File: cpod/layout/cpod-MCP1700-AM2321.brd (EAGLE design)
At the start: 14 parts, among them IC1 PCF8563DIP, Y1 32.768kHz

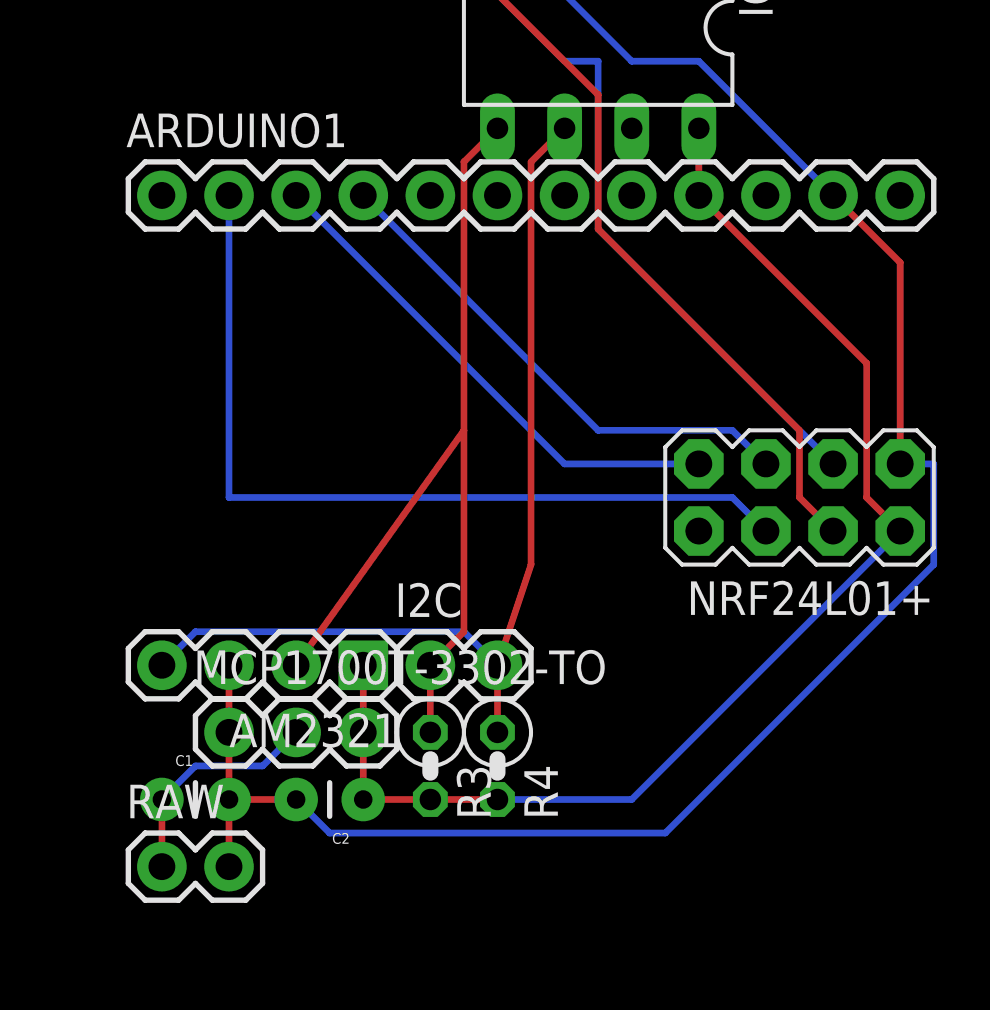
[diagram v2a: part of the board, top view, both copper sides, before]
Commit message: 增加了去耦电容
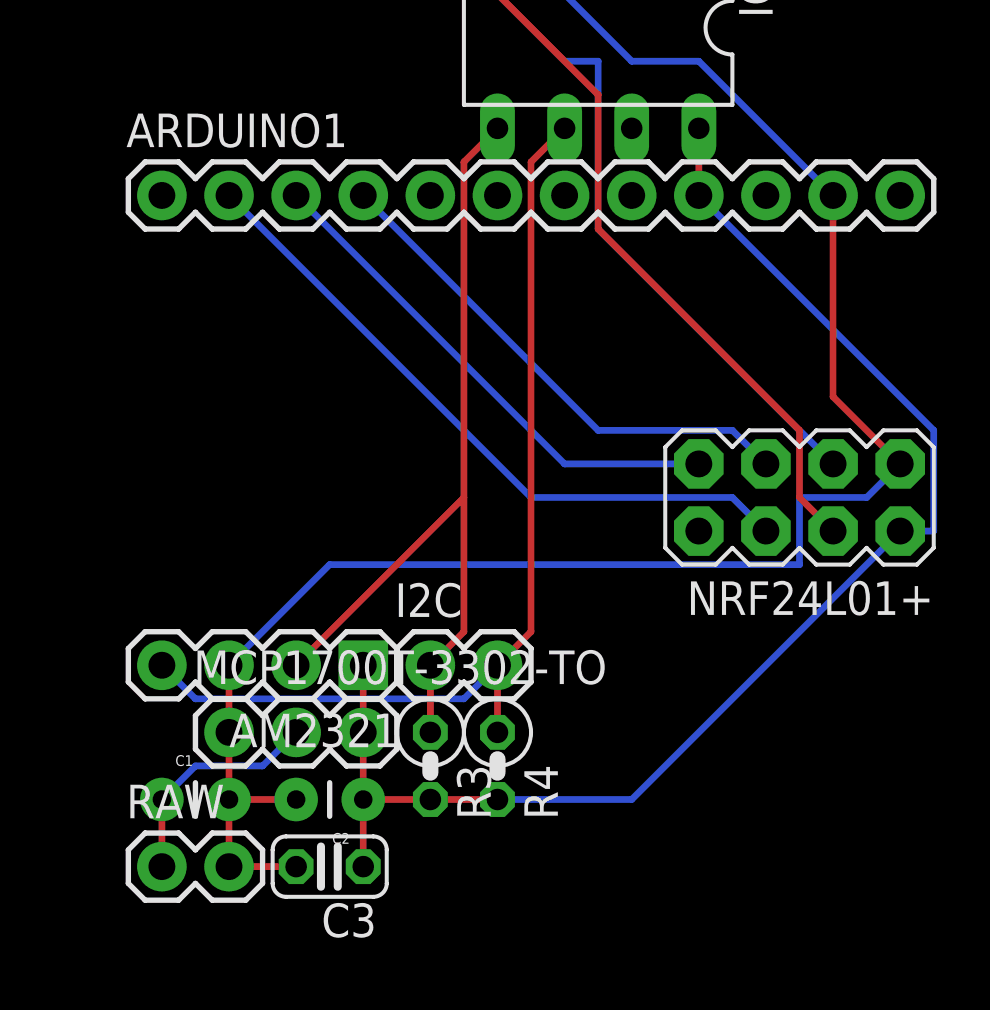
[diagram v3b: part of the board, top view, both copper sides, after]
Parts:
- added C3: 100nF, rcl:C025-024X044
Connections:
- net D3 renamed INT1
- net GND: now also C3.2
- net VCC: now also C3.1
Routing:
- net MOSI: track 32.3 -> 25.6 mm
- net VCC: track 48.0 -> 52.3 mm
- net SDA: track 34.8 -> 32.9 mm
- net GND: track 72.2 -> 70.9 mm
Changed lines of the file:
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@@
 <element name="IC1" library="CEDT" package="DIL08" value="PCF8563DIP" x="48.26" y="-10.16" rot="R180"/>
 <element name="Y1" library="SparkFun-FreqCtrl" package="TC26H" value="32.768kHz" x="50.8" y="-3.81"/>
+<element name="C3" library="rcl" package="C025-024X044" value="100nF" x="38.1" y="-41.91" rot="R180"/>
 </elements>
 <signals>
@@
 <wire x1="44.45" y1="-34.29" x2="44.45" y2="-36.83" width="0.254" layer="1"/>
 <wire x1="45.72" y1="-15.24" x2="46.99" y2="-13.97" width="0.254" layer="1"/>
-<wire x1="45.72" y1="-30.48" x2="45.72" y2="-15.24" width="0.254" layer="1"/>
-<wire x1="44.45" y1="-34.29" x2="45.72" y2="-30.48" width="0.254" layer="1"/>
-<wire x1="33.02" y1="-33.02" x2="31.75" y2="-34.29" width="0.254" layer="16"/>
-<wire x1="43.18" y1="-33.02" x2="33.02" y2="-33.02" width="0.254" layer="16"/>
-<wire x1="44.45" y1="-34.29" x2="43.18" y2="-33.02" width="0.254" layer="16"/>
+<wire x1="45.72" y1="-33.02" x2="45.72" y2="-15.24" width="0.254" layer="1"/>
+<wire x1="44.45" y1="-34.29" x2="45.72" y2="-33.02" width="0.254" layer="1"/>
+<wire x1="33.02" y1="-35.56" x2="31.75" y2="-34.29" width="0.254" layer="16"/>
+<wire x1="43.18" y1="-35.56" x2="33.02" y2="-35.56" width="0.254" layer="16"/>
+<wire x1="44.45" y1="-34.29" x2="43.18" y2="-35.56" width="0.254" layer="16"/>
 </signal>
 <signal name="GND">
@@
 <wire x1="52.07" y1="-11.43" x2="49.53" y2="-11.43" width="0.254" layer="16"/>
 <wire x1="57.15" y1="-16.51" x2="52.07" y2="-11.43" width="0.254" layer="16"/>
-<wire x1="59.69" y1="-19.05" x2="59.69" y2="-26.67" width="0.254" layer="1"/>
-<wire x1="57.15" y1="-16.51" x2="59.69" y2="-19.05" width="0.254" layer="1"/>
-<wire x1="38.1" y1="-40.64" x2="36.83" y2="-39.37" width="0.254" layer="16"/>
-<wire x1="50.8" y1="-40.64" x2="38.1" y2="-40.64" width="0.254" layer="16"/>
-<wire x1="60.96" y1="-30.48" x2="50.8" y2="-40.64" width="0.254" layer="16"/>
-<wire x1="60.96" y1="-26.67" x2="60.96" y2="-30.48" width="0.254" layer="16"/>
-<wire x1="59.69" y1="-26.67" x2="60.96" y2="-26.67" width="0.254" layer="16"/>
+<wire x1="57.15" y1="-24.13" x2="59.69" y2="-26.67" width="0.254" layer="1"/>
+<wire x1="57.15" y1="-16.51" x2="57.15" y2="-24.13" width="0.254" layer="1"/>
+<wire x1="38.1" y1="-30.48" x2="34.29" y2="-34.29" width="0.254" layer="16"/>
+<wire x1="55.88" y1="-30.48" x2="38.1" y2="-30.48" width="0.254" layer="16"/>
+<wire x1="55.88" y1="-27.94" x2="55.88" y2="-30.48" width="0.254" layer="16"/>
+<wire x1="58.42" y1="-27.94" x2="55.88" y2="-27.94" width="0.254" layer="16"/>
+<wire x1="59.69" y1="-26.67" x2="58.42" y2="-27.94" width="0.254" layer="16"/>
+<contactref element="C3" pad="2"/>
+<wire x1="34.29" y1="-41.91" x2="36.83" y2="-41.91" width="0.254" layer="1"/>
 </signal>
 <signal name="SDA">
@@
 <wire x1="41.91" y1="-34.29" x2="41.91" y2="-36.83" width="0.254" layer="1"/>
 <wire x1="43.18" y1="-15.24" x2="44.45" y2="-13.97" width="0.254" layer="1"/>
-<wire x1="43.18" y1="-33.02" x2="43.18" y2="-25.4" width="0.254" layer="1"/>
-<wire x1="43.18" y1="-25.4" x2="43.18" y2="-15.24" width="0.254" layer="1"/>
+<wire x1="43.18" y1="-33.02" x2="43.18" y2="-27.94" width="0.254" layer="1"/>
+<wire x1="43.18" y1="-27.94" x2="43.18" y2="-15.24" width="0.254" layer="1"/>
 <wire x1="41.91" y1="-34.29" x2="43.18" y2="-33.02" width="0.254" layer="1"/>
-<wire x1="43.18" y1="-25.4" x2="36.83" y2="-34.29" width="0.254" layer="1"/>
+<wire x1="43.18" y1="-27.94" x2="36.83" y2="-34.29" width="0.254" layer="1"/>
 </signal>
 <signal name="VCC">
@@
 <wire x1="49.53" y1="-39.37" x2="59.69" y2="-29.21" width="0.254" layer="16"/>
 <wire x1="44.45" y1="-39.37" x2="49.53" y2="-39.37" width="0.254" layer="16"/>
-<wire x1="58.42" y1="-22.86" x2="52.07" y2="-16.51" width="0.254" layer="1"/>
-<wire x1="58.42" y1="-27.94" x2="58.42" y2="-22.86" width="0.254" layer="1"/>
-<wire x1="59.69" y1="-29.21" x2="58.42" y2="-27.94" width="0.254" layer="1"/>
+<wire x1="60.96" y1="-25.4" x2="52.07" y2="-16.51" width="0.254" layer="16"/>
+<wire x1="60.96" y1="-29.21" x2="60.96" y2="-25.4" width="0.254" layer="16"/>
+<wire x1="59.69" y1="-29.21" x2="60.96" y2="-29.21" width="0.254" layer="16"/>
 <wire x1="39.37" y1="-39.37" x2="39.37" y2="-36.83" width="0.254" layer="1"/>
+<contactref element="C3" pad="1"/>
+<wire x1="39.37" y1="-39.37" x2="39.37" y2="-41.91" width="0.254" layer="1"/>
 </signal>
 <signal name="RAW">
@@
 <contactref element="ARDUINO1" pad="2"/>
 <contactref element="NRF24L01+" pad="6"/>
-<wire x1="34.29" y1="-27.94" x2="34.29" y2="-16.51" width="0.254" layer="16"/>
-<wire x1="53.34" y1="-27.94" x2="34.29" y2="-27.94" width="0.254" layer="16"/>
+<wire x1="45.72" y1="-27.94" x2="34.29" y2="-16.51" width="0.254" layer="16"/>
+<wire x1="53.34" y1="-27.94" x2="45.72" y2="-27.94" width="0.254" layer="16"/>
 <wire x1="54.61" y1="-29.21" x2="53.34" y2="-27.94" width="0.254" layer="16"/>
 </signal>
@@
 <contactref element="ARDUINO2" pad="11"/>
 </signal>
-<signal name="D3">
+<signal name="INT1">
 <contactref element="ARDUINO2" pad="7"/>
 </signal>

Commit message: I2C的上拉电阻改到5.1k
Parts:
- R3, R4: value 4.7k -> 5.1k
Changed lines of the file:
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@@
 <element name="RAW" library="SparkFun-Connectors" package="1X02" value="" x="31.75" y="-41.91"/>
 <element name="NRF24L01+" library="SparkFun-Connectors" package="2X4" value="M04X2" x="55.88" y="-27.94" rot="R180"/>
-<element name="R3" library="rcl" package="0207/2V" value="4.7k" x="41.91" y="-38.1" rot="R270"/>
-<element name="R4" library="rcl" package="0207/2V" value="4.7k" x="44.45" y="-38.1" rot="R270"/>
+<element name="R3" library="rcl" package="0207/2V" value="5.1k" x="41.91" y="-38.1" rot="R270"/>
+<element name="R4" library="rcl" package="0207/2V" value="5.1k" x="44.45" y="-38.1" rot="R270"/>
 <element name="I2C" library="SparkFun-Connectors" package="1X02" value="" x="41.91" y="-34.29"/>
 <element name="U$2" library="SparkFun-Aesthetics" package="OSHW-LOGO-L" value="" x="5.08" y="-38.1"/>

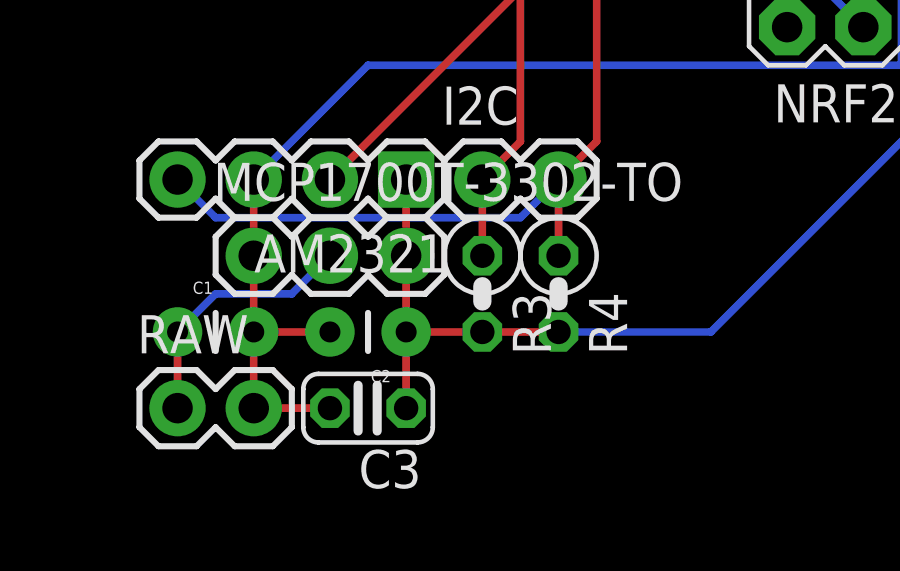
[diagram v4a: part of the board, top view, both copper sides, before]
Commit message: 把去耦放到电源框里，增加表意性。
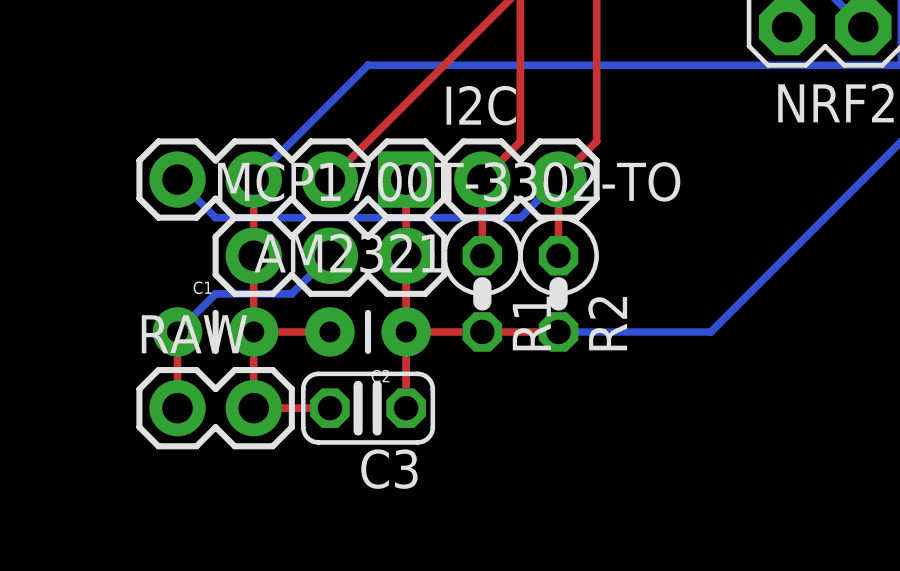
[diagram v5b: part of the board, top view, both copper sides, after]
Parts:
- renumbered R3 to R1, R4 to R2
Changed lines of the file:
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@@
 <element name="RAW" library="SparkFun-Connectors" package="1X02" value="" x="31.75" y="-41.91"/>
 <element name="NRF24L01+" library="SparkFun-Connectors" package="2X4" value="M04X2" x="55.88" y="-27.94" rot="R180"/>
-<element name="R3" library="rcl" package="0207/2V" value="5.1k" x="41.91" y="-38.1" rot="R270"/>
-<element name="R4" library="rcl" package="0207/2V" value="5.1k" x="44.45" y="-38.1" rot="R270"/>
+<element name="R1" library="rcl" package="0207/2V" value="5.1k" x="41.91" y="-38.1" rot="R270"/>
+<element name="R2" library="rcl" package="0207/2V" value="5.1k" x="44.45" y="-38.1" rot="R270"/>
 <element name="I2C" library="SparkFun-Connectors" package="1X02" value="" x="41.91" y="-34.29"/>
 <element name="U$2" library="SparkFun-Aesthetics" package="OSHW-LOGO-L" value="" x="5.08" y="-38.1"/>
@@
 <contactref element="AM2321" pad="4"/>
 <contactref element="I2C" pad="2"/>
-<contactref element="R4" pad="1"/>
+<contactref element="R2" pad="1"/>
 <contactref element="IC1" pad="6"/>
 <wire x1="44.45" y1="-34.29" x2="44.45" y2="-36.83" width="0.254" layer="1"/>
@@
 <contactref element="MCP1700T-3302-TO" pad="1"/>
 <contactref element="C1" pad="2"/>
-<contactref element="C2" pad="2"/>
 <contactref element="AM2321" pad="3"/>
 <contactref element="RAW" pad="2"/>
@@
 <contactref element="ARDUINO1" pad="11"/>
 <wire x1="34.29" y1="-36.83" x2="34.29" y2="-39.37" width="0.254" layer="1"/>
-<wire x1="34.29" y1="-39.37" x2="36.83" y2="-39.37" width="0.254" layer="1"/>
 <wire x1="34.29" y1="-39.37" x2="34.29" y2="-41.91" width="0.254" layer="1"/>
 <wire x1="34.29" y1="-36.83" x2="34.29" y2="-34.29" width="0.254" layer="1"/>
@@
 <wire x1="58.42" y1="-27.94" x2="55.88" y2="-27.94" width="0.254" layer="16"/>
 <wire x1="59.69" y1="-26.67" x2="58.42" y2="-27.94" width="0.254" layer="16"/>
+<contactref element="C2" pad="2"/>
 <contactref element="C3" pad="2"/>
 <wire x1="34.29" y1="-41.91" x2="36.83" y2="-41.91" width="0.254" layer="1"/>
+<wire x1="36.83" y1="-39.37" x2="34.29" y2="-39.37" width="0.254" layer="1"/>
 </signal>
 <signal name="SDA">
 <contactref element="AM2321" pad="2"/>
 <contactref element="I2C" pad="1"/>
-<contactref element="R3" pad="1"/>
+<contactref element="R1" pad="1"/>
 <contactref element="IC1" pad="5"/>
 <wire x1="41.91" y1="-34.29" x2="41.91" y2="-36.83" width="0.254" layer="1"/>
@@
 <contactref element="AM2321" pad="1"/>
 <contactref element="ARDUINO1" pad="9"/>
-<contactref element="C2" pad="1"/>
-<contactref element="R4" pad="2"/>
-<contactref element="R3" pad="2"/>
+<contactref element="R2" pad="2"/>
+<contactref element="R1" pad="2"/>
 <contactref element="NRF24L01+" pad="2"/>
 <contactref element="MCP1700T-3302-TO" pad="3"/>
@@
 <wire x1="39.37" y1="-34.29" x2="39.37" y2="-36.83" width="0.254" layer="1"/>
 <wire x1="52.07" y1="-16.51" x2="52.07" y2="-13.97" width="0.254" layer="1"/>
-<wire x1="39.37" y1="-39.37" x2="41.91" y2="-39.37" width="0.254" layer="1"/>
 <wire x1="41.91" y1="-39.37" x2="44.45" y2="-39.37" width="0.254" layer="1"/>
 <wire x1="49.53" y1="-39.37" x2="59.69" y2="-29.21" width="0.254" layer="16"/>
@@
 <wire x1="60.96" y1="-29.21" x2="60.96" y2="-25.4" width="0.254" layer="16"/>
 <wire x1="59.69" y1="-29.21" x2="60.96" y2="-29.21" width="0.254" layer="16"/>
-<wire x1="39.37" y1="-39.37" x2="39.37" y2="-36.83" width="0.254" layer="1"/>
+<contactref element="C2" pad="1"/>
 <contactref element="C3" pad="1"/>
 <wire x1="39.37" y1="-39.37" x2="39.37" y2="-41.91" width="0.254" layer="1"/>
+<wire x1="39.37" y1="-36.83" x2="39.37" y2="-39.37" width="0.254" layer="1"/>
+<wire x1="41.91" y1="-39.37" x2="39.37" y2="-39.37" width="0.254" layer="1"/>
 </signal>
 <signal name="RAW">
